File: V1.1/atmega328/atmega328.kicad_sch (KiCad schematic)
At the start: 24 parts, among them J1 Conn_01x04, J2 Conn_01x02, J3 Conn_01x02_Male, J4 Conn_01x03, J5 Conn_01x07, Q1 Si2319CDS, U1 ATmega328P-AU, U2 AS5048A, Y1 Crystal

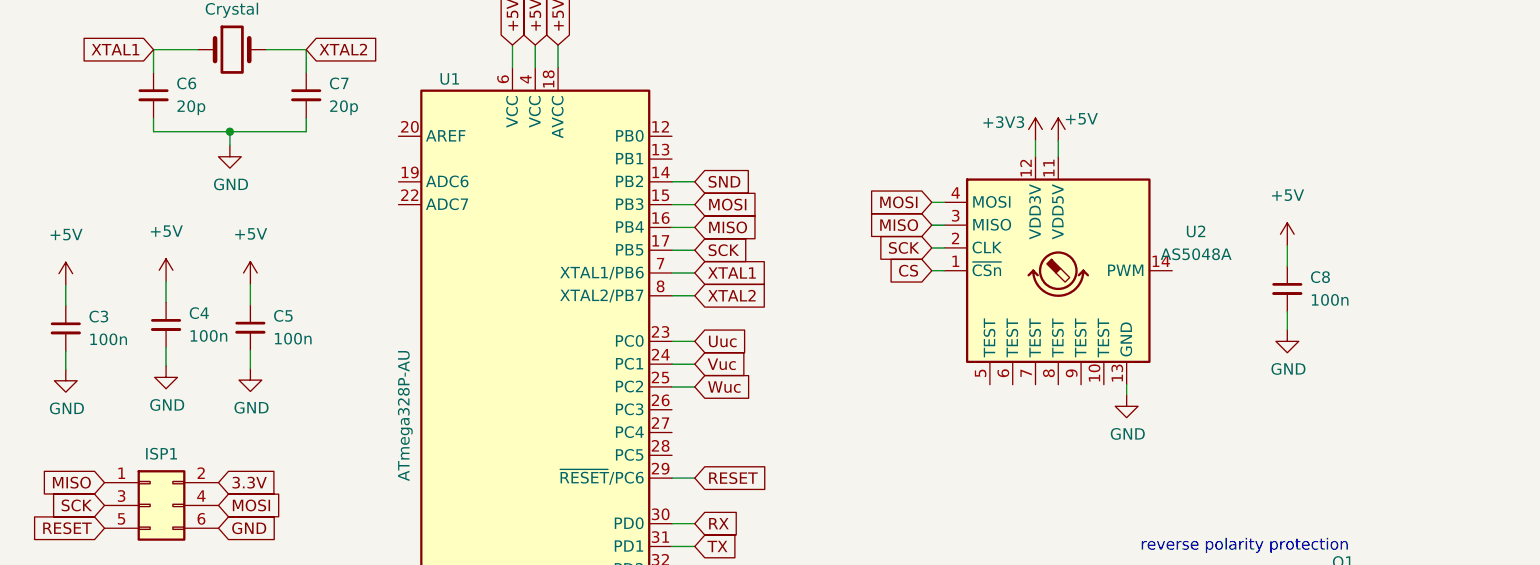
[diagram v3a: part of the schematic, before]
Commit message: recreating lost AS5048 version
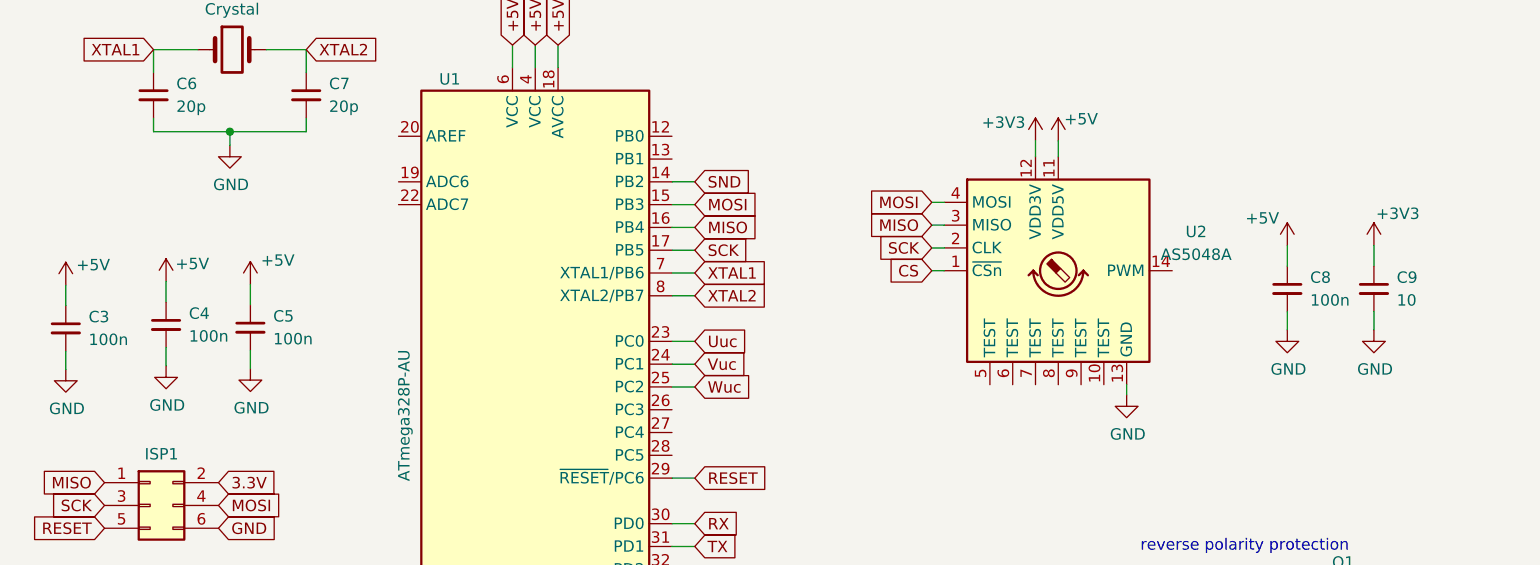
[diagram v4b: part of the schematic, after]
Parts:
- added C9: 10, Capacitor_SMD:C_0402_1005Metric, symbol Device:C_Small
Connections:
- net +3V3: now also C9.1
- net GND: now also C9.2
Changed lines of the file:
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@@
+    (stroke (width 0) (type default) (color 0 0 0 0))
+  )
+  (wire (pts (xy 168.402 51.689) (xy 168.402 53.721))
     (stroke (width 0) (type default) (color 0 0 0 0))
   )
@@
   )
   (wire (pts (xy 107.442 89.281) (xy 107.442 95.631))
+    (stroke (width 0) (type default) (color 0 0 0 0))
+  )
+  (wire (pts (xy 168.402 44.323) (xy 168.402 46.609))
     (stroke (width 0) (type default) (color 0 0 0 0))
   )
@@
   )
   (symbol (lib_id "power:+5V") (at 43.18 48.641 0) (unit 1)
-    (in_bom yes) (on_board yes) (fields_autoplaced)
+    (in_bom yes) (on_board yes)
     (property "Reference" "#PWR014" (id 0) (at 43.18 52.451 0)
       (effects (font (size 1.27 1.27)) hide)
     )
-    (property "Value" "+5V" (id 1) (at 43.18 43.053 0))
+    (property "Value" "+5V" (id 1) (at 46.228 45.974 0))
     (property "Footprint" "" (id 2) (at 43.18 48.641 0)
       (effects (font (size 1.27 1.27)) hide)
@@
   )
   (symbol (lib_id "power:+5V") (at 22.606 48.7162 0) (unit 1)
-    (in_bom yes) (on_board yes) (fields_autoplaced)
+    (in_bom yes) (on_board yes)
     (property "Reference" "#PWR01" (id 0) (at 22.606 52.5262 0)
       (effects (font (size 1.27 1.27)) hide)
     )
-    (property "Value" "+5V" (id 1) (at 22.606 43.1282 0))
+    (property "Value" "+5V" (id 1) (at 25.654 46.482 0))
     (property "Footprint" "" (id 2) (at 22.606 48.7162 0)
       (effects (font (size 1.27 1.27)) hide)
@@
   )
   (symbol (lib_id "power:+5V") (at 158.75 44.323 0) (unit 1)
-    (in_bom yes) (on_board yes) (fields_autoplaced)
+    (in_bom yes) (on_board yes)
     (property "Reference" "#PWR0104" (id 0) (at 158.75 48.133 0)
       (effects (font (size 1.27 1.27)) hide)
     )
-    (property "Value" "+5V" (id 1) (at 158.75 38.735 0))
+    (property "Value" "+5V" (id 1) (at 155.956 41.275 0))
     (property "Footprint" "" (id 2) (at 158.75 44.323 0)
       (effects (font (size 1.27 1.27)) hide)
@@
     (pin "1")
   )
+  (symbol (lib_id "power:+3V3") (at 168.402 44.323 0) (unit 1)
+    (in_bom yes) (on_board yes)
+    (property "Reference" "#PWR03" (id 0) (at 168.402 48.133 0)
+      (effects (font (size 1.27 1.27)) hide)
+    )
+    (property "Value" "+3V3" (id 1) (at 171.069 40.767 0))
+    (property "Footprint" "" (id 2) (at 168.402 44.323 0)
+      (effects (font (size 1.27 1.27)) hide)
+    )
+    (property "Datasheet" "" (id 3) (at 168.402 44.323 0)
+      (effects (font (size 1.27 1.27)) hide)
+    )
+    (pin "1")
+  )
+  (symbol (lib_id "Device:C_Small") (at 168.402 49.149 0) (unit 1)
+    (in_bom yes) (on_board yes)
+    (property "Reference" "C9" (id 0) (at 170.942 47.879 0)
+      (effects (font (size 1.27 1.27)) (justify left))
+    )
+    (property "Value" "10" (id 1) (at 170.942 50.419 0)
+      (effects (font (size 1.27 1.27)) (justify left))
+    )
+    (property "Footprint" "Capacitor_SMD:C_0402_1005Metric" (id 2) (at 168.402 49.149 0)
+      (effects (font (size 1.27 1.27)) hide)
+    )
+    (property "Datasheet" "https://datasheet.lcsc.com/lcsc/1810191219_Samsung-Electro-Mechanics-CL05B104KO5NNNC_C1525.pdf" (id 3) (at 168.402 49.149 0)
+      (effects (font (size 1.27 1.27)) hide)
+    )
+    (property "LCSC" "C1525" (id 6) (at 168.402 49.149 0)
+      (effects (font (size 1.27 1.27)) hide)
+    )
+    (pin "1")
+    (pin "2")
+  )
   (symbol (lib_id "Diode:BZV55B10") (at 170.053 88.519 270) (unit 1)
     (in_bom yes) (on_board yes) (fields_autoplaced)
@@
     (pin "2")
   )
+  (symbol (lib_id "power:GND") (at 168.402 53.721 0) (unit 1)
+    (in_bom yes) (on_board yes)
+    (property "Reference" "#PWR04" (id 0) (at 168.402 60.071 0)
+      (effects (font (size 1.27 1.27)) hide)
+    )
+    (property "Value" "GND" (id 1) (at 168.529 58.1152 0))
+    (property "Footprint" "" (id 2) (at 168.402 53.721 0)
+      (effects (font (size 1.27 1.27)) hide)
+    )
+    (property "Datasheet" "" (id 3) (at 168.402 53.721 0)
+      (effects (font (size 1.27 1.27)) hide)
+    )
+    (pin "1")
+  )
   (symbol (lib_id "Device:R_Small") (at 23.114 99.695 180) (unit 1)
     (in_bom yes) (on_board yes)
@@
   )
   (symbol (lib_id "power:+5V") (at 33.782 48.3352 0) (unit 1)
-    (in_bom yes) (on_board yes) (fields_autoplaced)
+    (in_bom yes) (on_board yes)
     (property "Reference" "#PWR07" (id 0) (at 33.782 52.1452 0)
       (effects (font (size 1.27 1.27)) hide)
     )
-    (property "Value" "+5V" (id 1) (at 33.782 42.7472 0))
+    (property "Value" "+5V" (id 1) (at 36.703 46.355 0))
     (property "Footprint" "" (id 2) (at 33.782 48.3352 0)
       (effects (font (size 1.27 1.27)) hide)
@@
       (reference "#PWR02") (unit 1) (value "GND") (footprint "")
     )
+    (path "/97a5a1a5-4adb-4603-b200-5996ce071169"
+      (reference "#PWR03") (unit 1) (value "+3V3") (footprint "")
+    )
+    (path "/a2d1f862-abff-4911-8ca4-fe733d244d8c"
+      (reference "#PWR04") (unit 1) (value "GND") (footprint "")
+    )
     (path "/e46660af-be56-44c6-a3b9-0c44eb041a47"
       (reference "#PWR07") (unit 1) (value "+5V") (footprint "")
@@
       (reference "C8") (unit 1) (value "100n") (footprint "Capacitor_SMD:C_0402_1005Metric")
     )
+    (path "/993dfb4b-2de0-42e1-ac4d-b11207eab642"
+      (reference "C9") (unit 1) (value "10") (footprint "Capacitor_SMD:C_0402_1005Metric")
+    )
     (path "/9d4896c0-71c0-408c-a483-cfbfb4cd54b4"

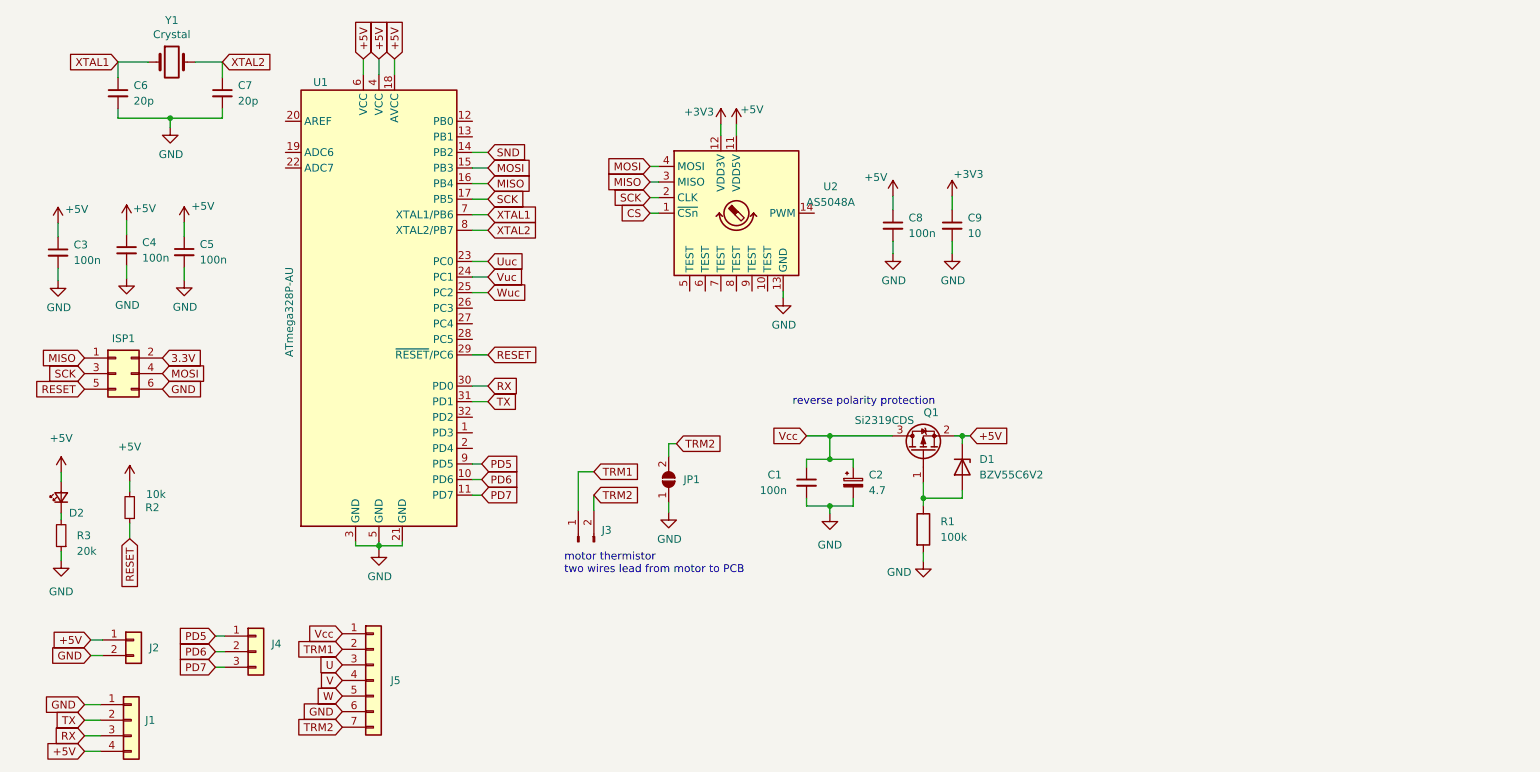
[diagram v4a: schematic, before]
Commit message: recreating lost AS5048 version
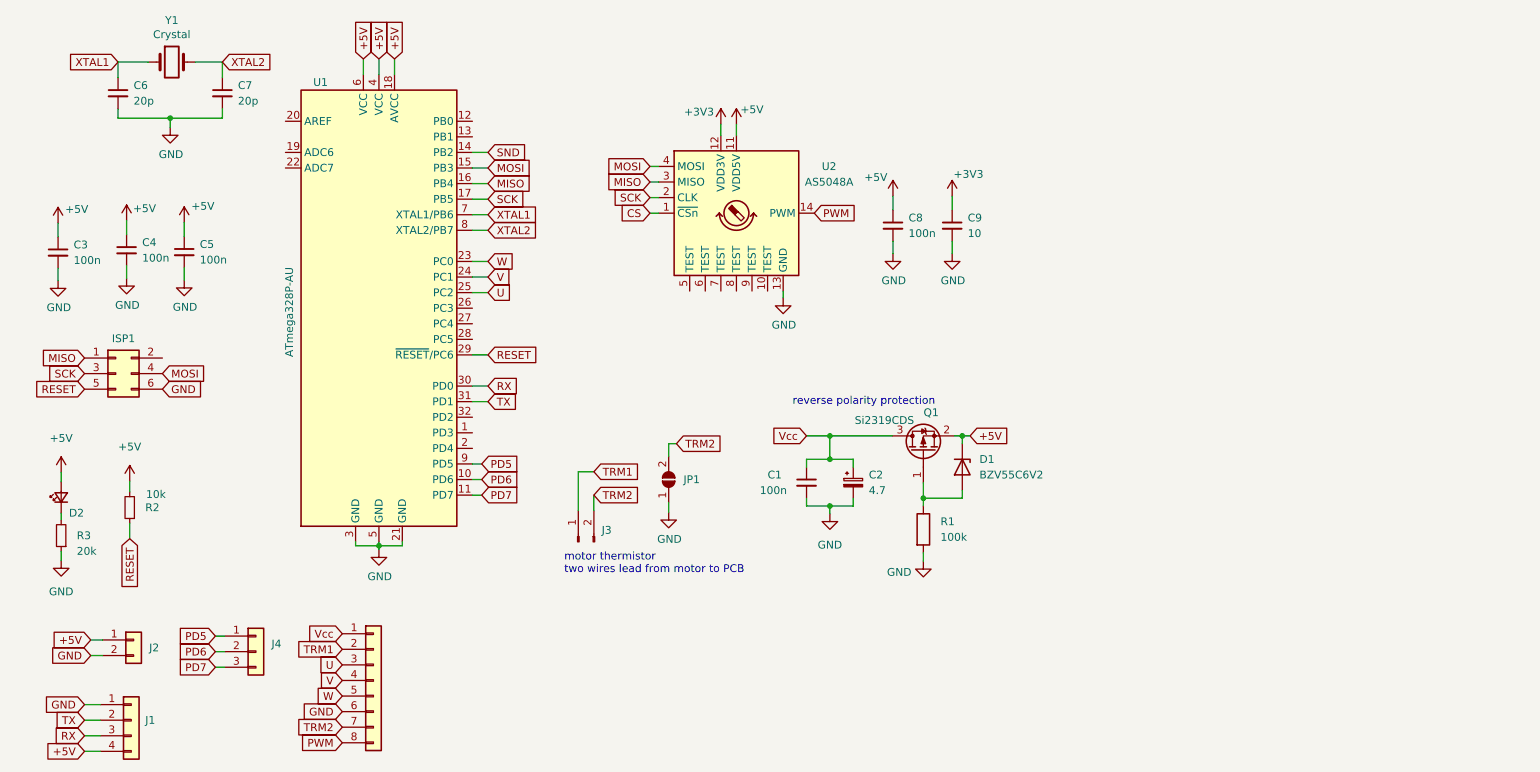
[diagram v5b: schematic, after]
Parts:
- removed J5: Conn_01x07, symbol Connector_Generic:Conn_01x07
- added J5: Conn_01x08, Connector_PinHeader_2.54mm:PinHeader_1x08_P2.54mm_Vertical, symbol Connector_Generic:Conn_01x08
- J1: footprint (none) -> Connector_PinHeader_2.54mm:PinHeader_1x04_P2.54mm_Vertical
- J2: footprint (none) -> Connector_PinHeader_2.54mm:myPinHeader_1x02_P2.54mm_Vertical
- J4: footprint (none) -> Connector_PinHeader_2.54mm:PinHeader_1x03_P2.54mm_Vertical
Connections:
- net Uuc is gone; now on net W: U1.23 (PC0)
- net Vuc is gone; now on net V: U1.24 (PC1)
- net Wuc is gone; now on net U: U1.25 (PC2)
- net GND: now also J5.6 (Pin_6)
- net TRM1: now also J5.2 (Pin_2)
- net TRM2: now also J5.7 (Pin_7)
- net U: now also J5.3 (Pin_3)
- net V: now also J5.4 (Pin_4)
- net Vcc: now also J5.1 (Pin_1)
- net W: now also J5.5 (Pin_5)
- net PWM: now reaches U2.14 (PWM)
- net PWM: now also J5.8 (Pin_8)
- net 3.3V: no longer names the net of ISP1.2 (Pin_2)
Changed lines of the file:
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@@
+    )
+  )
+  (global_label "PWM" (shape input) (at 68.961 133.477 180) (fields_autoplaced)
+    (effects (font (size 1.27 1.27)) (justify right))
+    (property "Intersheet References" "${INTERSHEET_REFS}" (id 0) (at 62.4639 133.3976 0)
+      (effects (font (size 1.27 1.27)) (justify right) hide)
     )
   )
@@
     )
   )
-  (global_label "3.3V" (shape input) (at 39.624 70.739 0) (fields_autoplaced)
-    (effects (font (size 1.27 1.27)) (justify left))
-    (property "Intersheet References" "${INTERSHEET_REFS}" (id 0) (at 106.299 -70.866 0)
-      (effects (font (size 1.27 1.27)) hide)
-    )
-  )
   (global_label "+5V" (shape input) (at 74.93 21.971 90) (fields_autoplaced)
     (effects (font (size 1.27 1.27)) (justify left))
@@
     )
   )
-  (global_label "Wuc" (shape input) (at 92.71 60.071 0) (fields_autoplaced)
-    (effects (font (size 1.27 1.27)) (justify left))
-    (property "Intersheet References" "${INTERSHEET_REFS}" (id 0) (at 98.7232 59.9916 0)
+  (global_label "U" (shape input) (at 92.71 60.071 0) (fields_autoplaced)
+    (effects (font (size 1.27 1.27)) (justify left))
+    (property "Intersheet References" "${INTERSHEET_REFS}" (id 0) (at 96.3647 59.9916 0)
       (effects (font (size 1.27 1.27)) (justify left) hide)
     )
@@
     )
   )
+  (global_label "PWM" (shape input) (at 145.923 47.117 0) (fields_autoplaced)
+    (effects (font (size 1.27 1.27)) (justify left))
+    (property "Intersheet References" "${INTERSHEET_REFS}" (id 0) (at 152.4201 47.0376 0)
+      (effects (font (size 1.27 1.27)) (justify left) hide)
+    )
+  )
   (global_label "RESET" (shape input) (at 34.29 100.203 270) (fields_autoplaced)
     (effects (font (size 1.27 1.27)) (justify right))
@@
     )
   )
-  (global_label "Uuc" (shape input) (at 92.71 54.991 0) (fields_autoplaced)
-    (effects (font (size 1.27 1.27)) (justify left))
-    (property "Intersheet References" "${INTERSHEET_REFS}" (id 0) (at 98.6023 54.9116 0)
+  (global_label "W" (shape input) (at 92.71 54.991 0) (fields_autoplaced)
+    (effects (font (size 1.27 1.27)) (justify left))
+    (property "Intersheet References" "${INTERSHEET_REFS}" (id 0) (at 96.4856 54.9116 0)
       (effects (font (size 1.27 1.27)) (justify left) hide)
     )
@@
     )
   )
-  (global_label "Vuc" (shape input) (at 92.71 57.531 0) (fields_autoplaced)
-    (effects (font (size 1.27 1.27)) (justify left))
-    (property "Intersheet References" "${INTERSHEET_REFS}" (id 0) (at 98.3604 57.4516 0)
+  (global_label "V" (shape input) (at 92.71 57.531 0) (fields_autoplaced)
+    (effects (font (size 1.27 1.27)) (justify left))
+    (property "Intersheet References" "${INTERSHEET_REFS}" (id 0) (at 96.1228 57.4516 0)
       (effects (font (size 1.27 1.27)) (justify left) hide)
     )
@@
       (effects (font (size 1.27 1.27)) (justify left) hide)
     )
-    (property "Footprint" "" (id 2) (at 34.544 129.794 0)
+    (property "Footprint" "Connector_PinHeader_2.54mm:PinHeader_1x04_P2.54mm_Vertical" (id 2) (at 34.544 129.794 0)
       (effects (font (size 1.27 1.27)) hide)
     )
@@
       (effects (font (size 1.27 1.27)) (justify left) hide)
     )
-    (property "Footprint" "" (id 2) (at 54.864 118.618 0)
+    (property "Footprint" "Connector_PinHeader_2.54mm:PinHeader_1x03_P2.54mm_Vertical" (id 2) (at 54.864 118.618 0)
       (effects (font (size 1.27 1.27)) hide)
     )
@@
     (pin "1")
   )
-  (symbol (lib_id "Connector_Generic:Conn_01x07") (at 74.041 123.317 0) (unit 1)
+  (symbol (lib_id "Connector_Generic:Conn_01x08") (at 74.041 123.317 0) (unit 1)
     (in_bom yes) (on_board yes) (fields_autoplaced)
-    (property "Reference" "J5" (id 0) (at 76.835 123.3169 0)
-      (effects (font (size 1.27 1.27)) (justify left))
-    )
-    (property "Value" "Conn_01x07" (id 1) (at 77.089 124.5869 0)
-      (effects (font (size 1.27 1.27)) (justify left) hide)
-    )
-    (property "Footprint" "" (id 2) (at 74.041 123.317 0)
+    (property "Reference" "J5" (id 0) (at 76.073 123.3169 0)
+      (effects (font (size 1.27 1.27)) (justify left) hide)
+    )
+    (property "Value" "Conn_01x08" (id 1) (at 76.2 124.5869 0)
+      (effects (font (size 1.27 1.27)) (justify left) hide)
+    )
+    (property "Footprint" "Connector_PinHeader_2.54mm:PinHeader_1x08_P2.54mm_Vertical" (id 2) (at 74.041 123.317 0)
       (effects (font (size 1.27 1.27)) hide)
     )
@@
     (pin "6")
     (pin "7")
+    (pin "8")
   )
   (symbol (lib_id "power:+5V") (at 158.75 44.323 0) (unit 1)
@@
       (effects (font (size 1.27 1.27)) (justify left) hide)
     )
-    (property "Footprint" "" (id 2) (at 34.925 116.713 0)
+    (property "Footprint" "Connector_PinHeader_2.54mm:myPinHeader_1x02_P2.54mm_Vertical" (id 2) (at 34.925 116.713 0)
       (effects (font (size 1.27 1.27)) hide)
     )
@@
   )
   (symbol (lib_id "Sensor_Magnetic:AS5048A") (at 133.223 47.117 0) (unit 1)
-    (in_bom yes) (on_board yes) (fields_autoplaced)
-    (property "Reference" "U2" (id 0) (at 148.59 42.7863 0))
-    (property "Value" "AS5048A" (id 1) (at 148.59 45.3263 0))
+    (in_bom yes) (on_board yes)
+    (property "Reference" "U2" (id 0) (at 148.336 39.497 0))
+    (property "Value" "AS5048A" (id 1) (at 148.336 42.037 0))
     (property "Footprint" "Package_SO:TSSOP-14_4.4x5mm_P0.65mm" (id 2) (at 133.223 66.167 0)
       (effects (font (size 1.27 1.27)) hide)
@@
     )
     (path "/04013dca-8116-4a03-b1b1-6aad3eddb36d"
-      (reference "J1") (unit 1) (value "Conn_01x04") (footprint "")
+      (reference "J1") (unit 1) (value "Conn_01x04") (footprint "Connector_PinHeader_2.54mm:PinHeader_1x04_P2.54mm_Vertical")
     )
     (path "/7a55b174-5cc7-4525-80d2-2644b42a21b5"
-      (reference "J2") (unit 1) (value "Conn_01x02") (footprint "")
+      (reference "J2") (unit 1) (value "Conn_01x02") (footprint "Connector_PinHeader_2.54mm:myPinHeader_1x02_P2.54mm_Vertical")
     )
     (path "/55f70e6c-6342-4715-b8ba-c17f5a663a44"
@@
     )
     (path "/56107381-a1b3-4be1-8d54-6548558abaee"
-      (reference "J4") (unit 1) (value "Conn_01x03") (footprint "")
-    )
-    (path "/745777f8-386e-40f8-91e4-c09e2aa5a715"
-      (reference "J5") (unit 1) (value "Conn_01x07") (footprint "")
+      (reference "J4") (unit 1) (value "Conn_01x03") (footprint "Connector_PinHeader_2.54mm:PinHeader_1x03_P2.54mm_Vertical")
+    )
+    (path "/703cce26-4ed2-4985-a67f-4839a6d7a951"
+      (reference "J5") (unit 1) (value "Conn_01x08") (footprint "Connector_PinHeader_2.54mm:PinHeader_1x08_P2.54mm_Vertical")
     )
     (path "/38403b41-e4dd-4954-8433-1dfbff3a0ed0"
